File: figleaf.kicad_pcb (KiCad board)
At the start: 2 copper layers, 145 x 105 mm, 70 parts, among them J1 Conn_01x02_Pin, J2 HRO_TYPE-C-31-M-14, J3 Battery, J9 TC2030_SWD, Q2 2N7002, SW1 PWR, SW2 RST, U1 SRV05-4, U10 MAX17048, U3 BQ24075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

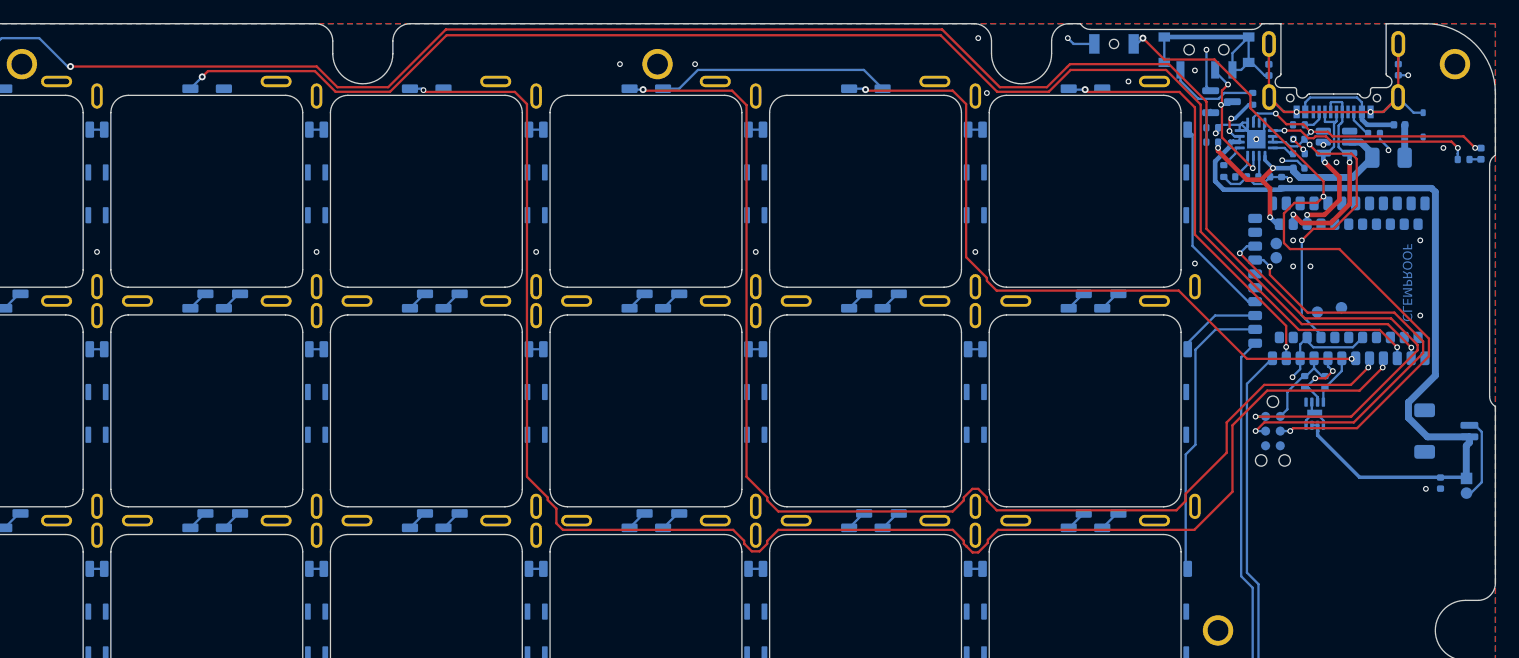
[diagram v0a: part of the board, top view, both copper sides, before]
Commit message: Move MCU inwards, for the last time pls bro
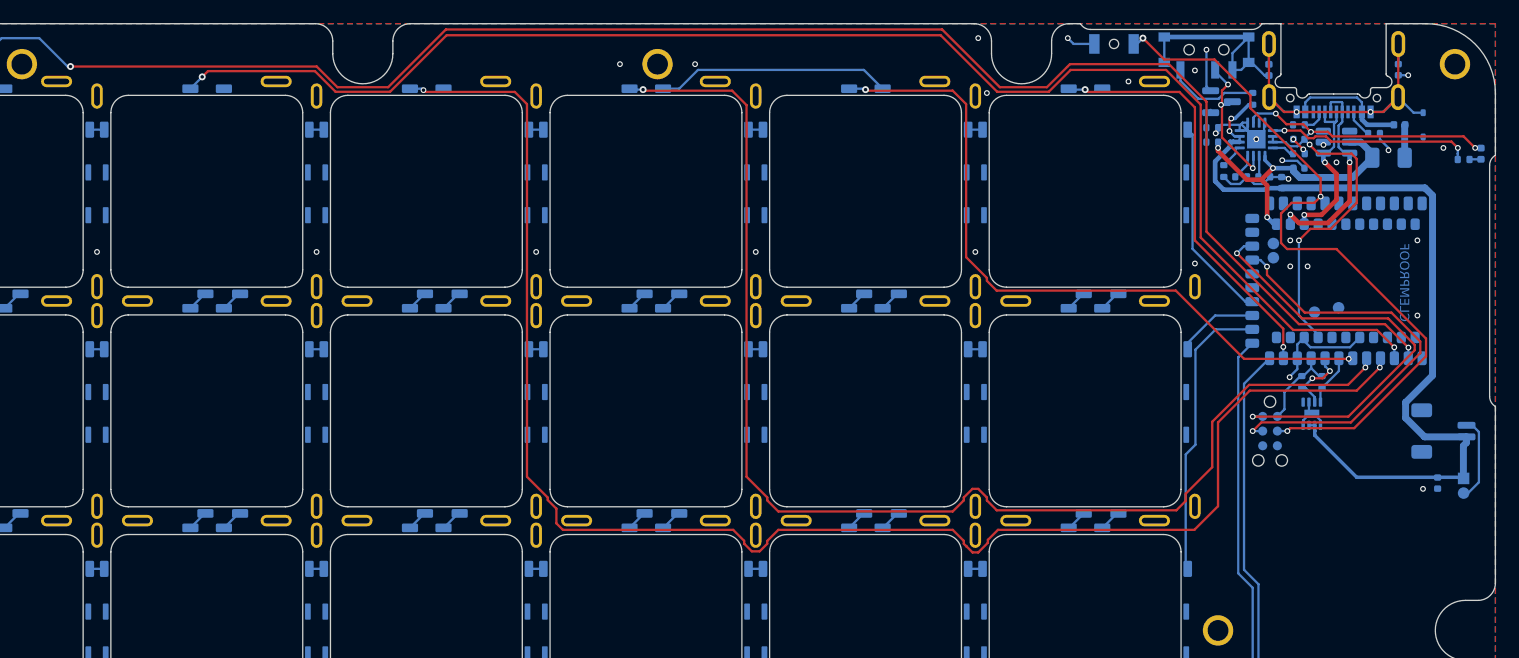
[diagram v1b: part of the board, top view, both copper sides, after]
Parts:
- moved C17 0.25 mm to (152.5, 52.2)
- moved J1 0.25 mm to (154.8, 51.8)
- moved J3 0.25 mm to (153.0, 47.8)
- moved J9 0.25 mm to (138.0, 47.8)
- moved R18 0.25 mm to (142.5, 43.5)
- moved R19 0.25 mm to (140.8, 43.5)
- moved U10 0.25 mm to (141.6, 46.2)
- moved U8 0.25 mm to (146.8, 34.8)
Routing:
- net col_2: track 133.5 -> 134.1 mm
- net col_3: track 107.8 -> 108.3 mm

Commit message: Move XY to better coord
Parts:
- moved U8 17.7 mm to (134.2, 22.2)
- moved Q2 17.7 mm to (121.3, 6.75)
- moved C1 17.7 mm to (136.6, 3.98)
- moved C17 17.7 mm to (140.0, 39.8)
- moved C5 17.7 mm to (128.0, 12.5)
- moved C6 17.7 mm to (128.0, 10.0)
- moved C7 17.7 mm to (126.5, 13.8)
- moved D1 17.7 mm to (138.8, 8.75)
- moved F1 17.7 mm to (135.8, 11.6)
- moved H1 17.7 mm to (17.5, 3.50)
- moved H2 17.7 mm to (72.5, 3.50)
- moved H3 17.7 mm to (141.5, 3.50)
- moved H4 17.7 mm to (121.0, 52.5)
- moved H5 17.7 mm to (141.5, 101.5)
- moved H6 17.7 mm to (72.5, 101.5)
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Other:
- outline, holes or cut-outs redrawn

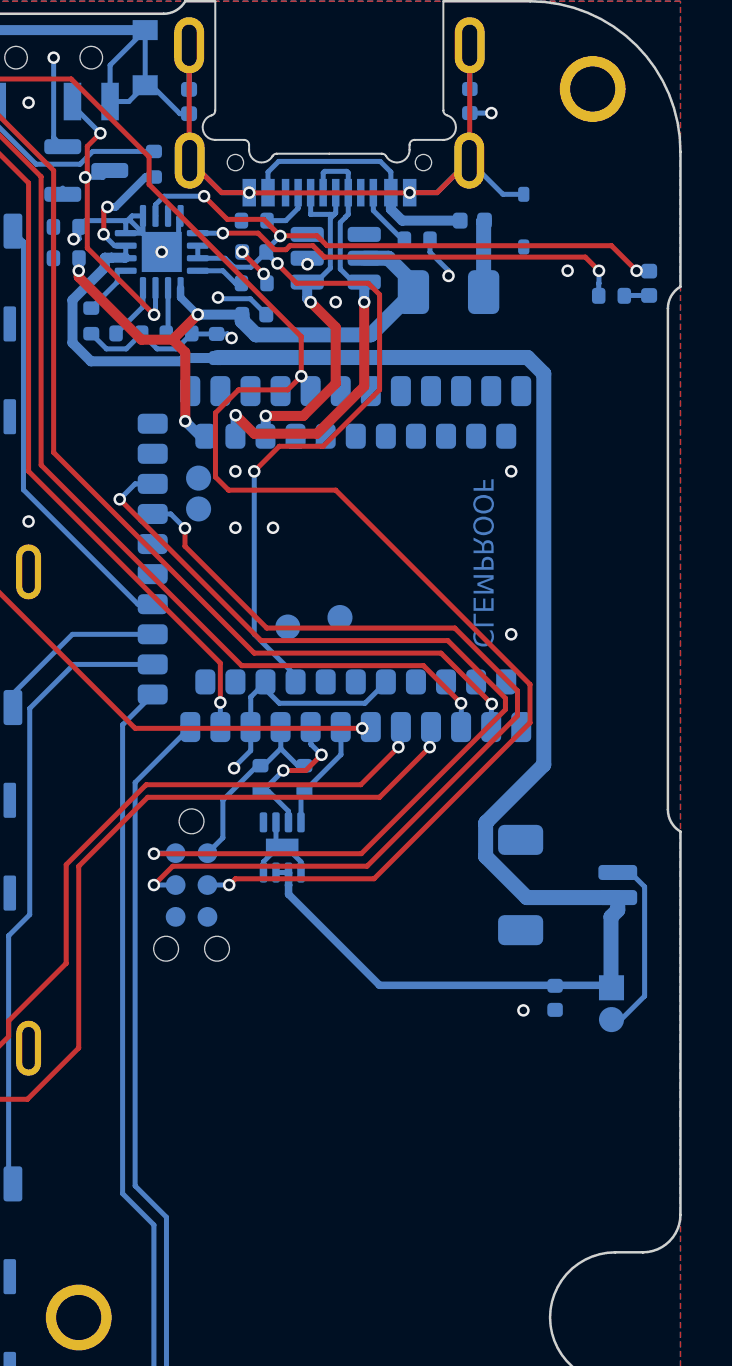
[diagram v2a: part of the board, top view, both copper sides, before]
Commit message: adjust mcu cutout
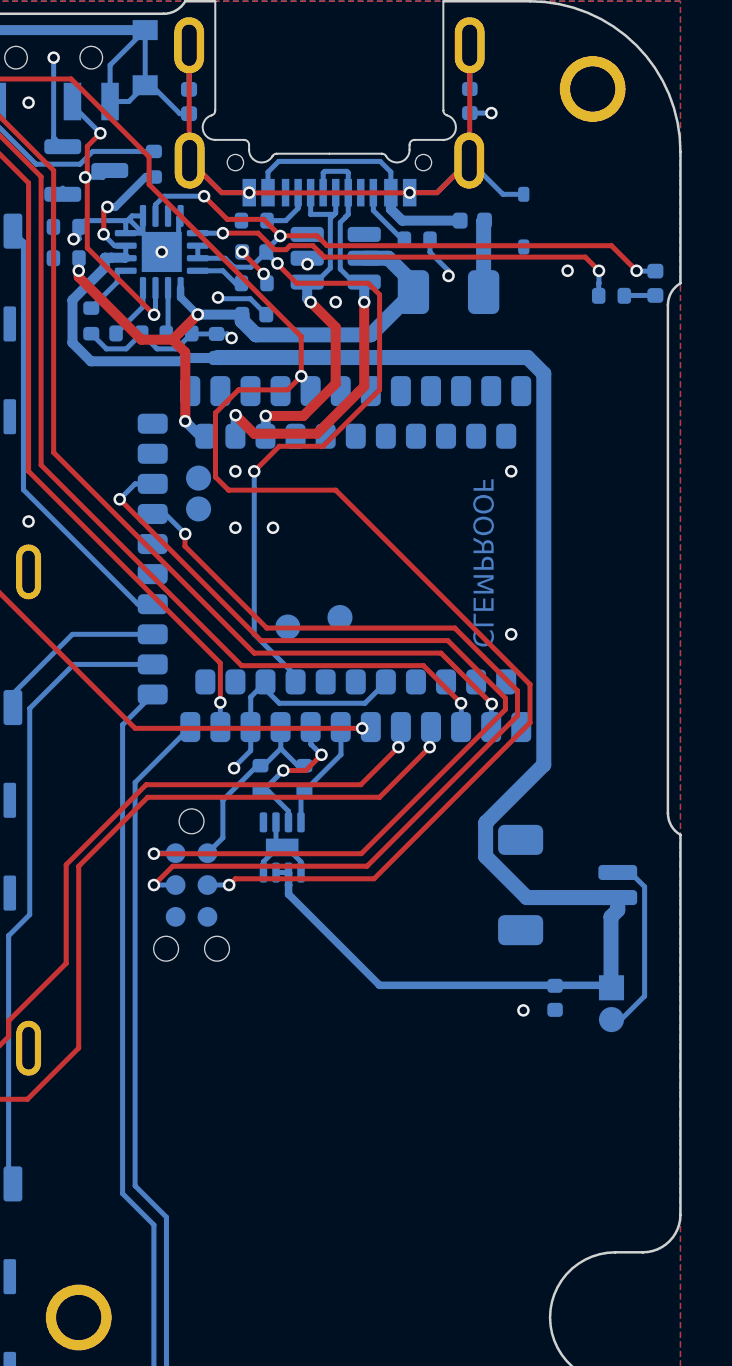
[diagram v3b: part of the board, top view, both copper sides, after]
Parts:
- moved LED2 0.25 mm to (144.0, 11.2)
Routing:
- net +VSW: track 50.6 -> 51.1 mm
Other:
- outline, holes or cut-outs redrawn

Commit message: move vias
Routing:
- net GND_L: track 89.8 -> 90.2 mm, vias 37 -> 38

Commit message: testing m2 mounting holes
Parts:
- H1, H2, H3, H4, H5, H6, H7: footprint Graz_Footprints:m1.6 -> Graz_Footprints:MountingHole_M2_Graz
- moved H4 1.00 mm to (122.0, 52.5)
- moved H1 0.50 mm to (17.5, 3.00)
- moved H2 0.50 mm to (72.5, 3.00)
- moved H6 0.50 mm to (72.5, 102.0)
- moved H7 0.50 mm to (17.5, 102.0)
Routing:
- net col_0: track 151.6 -> 152.9 mm
- net row_4: track 60.2 -> 61.0 mm
- net row_3: track 41.9 -> 42.7 mm

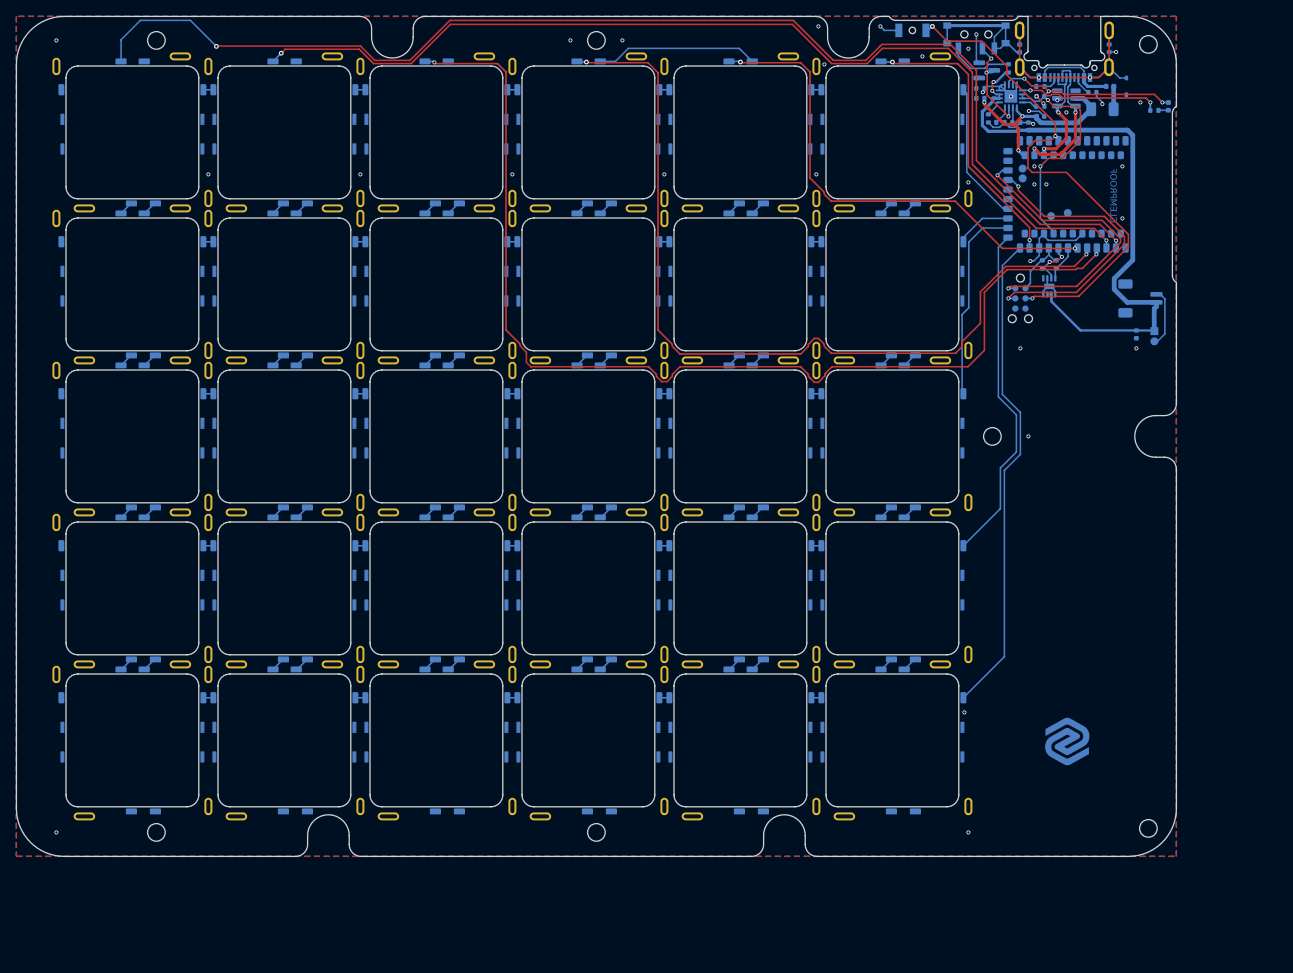
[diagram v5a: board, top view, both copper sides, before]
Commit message: finish m2 refactor
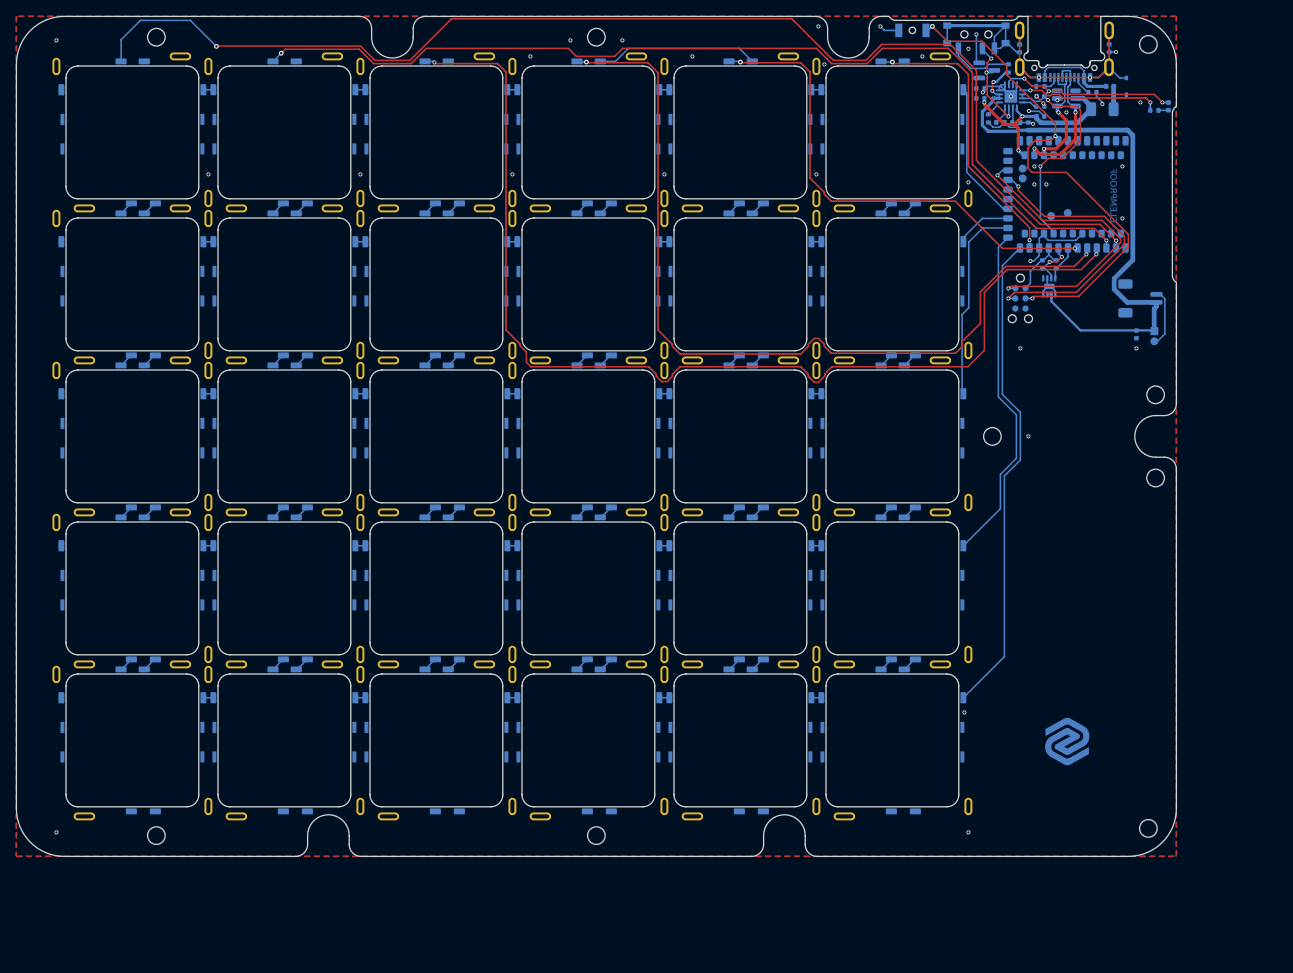
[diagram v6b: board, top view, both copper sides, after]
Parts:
- added H8: MountingHole, Graz_Footprints:MountingHole_M2_Graz, F.Cu at (17.5, 102.4)
- added H9: MountingHole, Graz_Footprints:MountingHole_M2_Graz, F.Cu at (122.0, 52.5)
- moved H6 69.0 mm to (141.5, 101.5)
- moved H7 55.0 mm to (72.5, 102.4)
- moved H5 43.8 mm to (142.4, 57.7)
- moved H4 21.1 mm to (142.4, 47.3)
- moved H1 0.40 mm to (17.5, 2.60)
- moved H2 0.40 mm to (72.5, 2.60)
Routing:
- net col_1: track 128.0 -> 126.4 mm
- net GND_L: vias 38 -> 40
